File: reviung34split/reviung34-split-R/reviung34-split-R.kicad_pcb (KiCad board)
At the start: 2 copper layers, 100 x 100 mm, 38 parts, among them J1 8P8C, SW19 SW_PUSH, SW20 SW_PUSH, SW21 SW_PUSH, SW22 SW_PUSH, SW23 SW_PUSH, SW24 SW_PUSH, SW25 SW_PUSH, SW26 SW_PUSH, SW27 SW_PUSH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

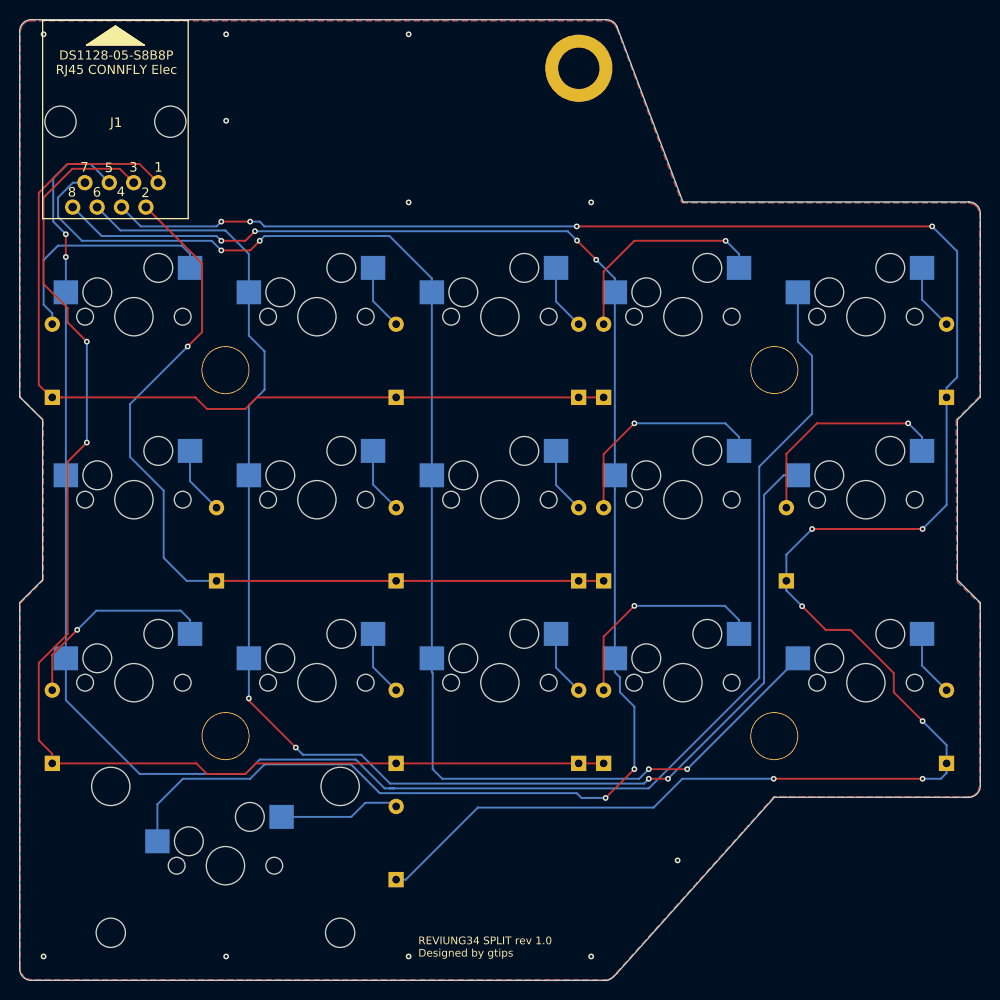
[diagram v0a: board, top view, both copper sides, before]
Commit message: RJ45_NONAME_8P8C_Horizontal
Redone with very common RJ45_NONAME_8P8C_Horizontal socket's footprint and KiCad 6.0.4.
https://aliexpress.ru/item/32774556179.html
https://aliexpress.ru/item/4001295248605.html
https://aliexpress.ru/item/32694863099.html
https://aliexpress.ru/item/32902228456.html
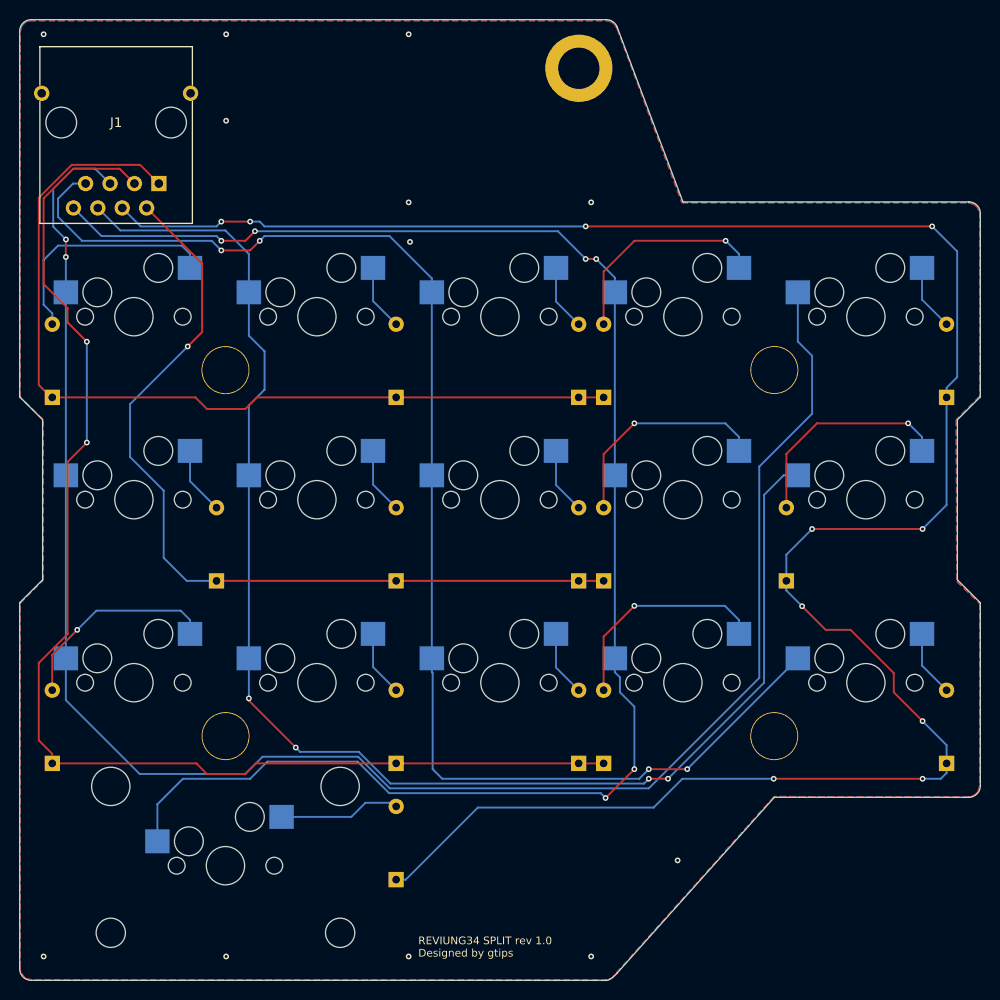
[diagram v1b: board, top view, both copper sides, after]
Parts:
- J1: footprint _reviung-kbd:RJ45-DS1128-05-S8B8P -> Connector_NONAME:RJ45_NONAME_8P8C_Horizontal
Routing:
- net col5: track 187.7 -> 186.5 mm
- net col6: track 151.9 -> 151.0 mm
- net col7: track 143.5 -> 143.0 mm
- net GND: vias 11 -> 12
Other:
- net class Default removed
